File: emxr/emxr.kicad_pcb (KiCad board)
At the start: 2 copper layers, 167.9 x 76.5 mm, 137 parts, among them IC201 NJM4558D, IC301 NJM4556D, IC401 NJM2068DD, IC402 NJM4580, IC501 NJM2068DD, IC502 NJM4580, J101 POWER, J103 Bus Conn, J104 GEQ_L_PRE, J105 GEQ_L_POST, J106 GEQ_R_PRE, J107 GEQ_R_POST, J108 AUDIO_OUT, J205 InpVolL, J206 InpVolR, J208 SrcSel, J301 HPHONES, J302 HPVolL, J303 HPVolR, J401 FrontVolL, J501 FrontVolL

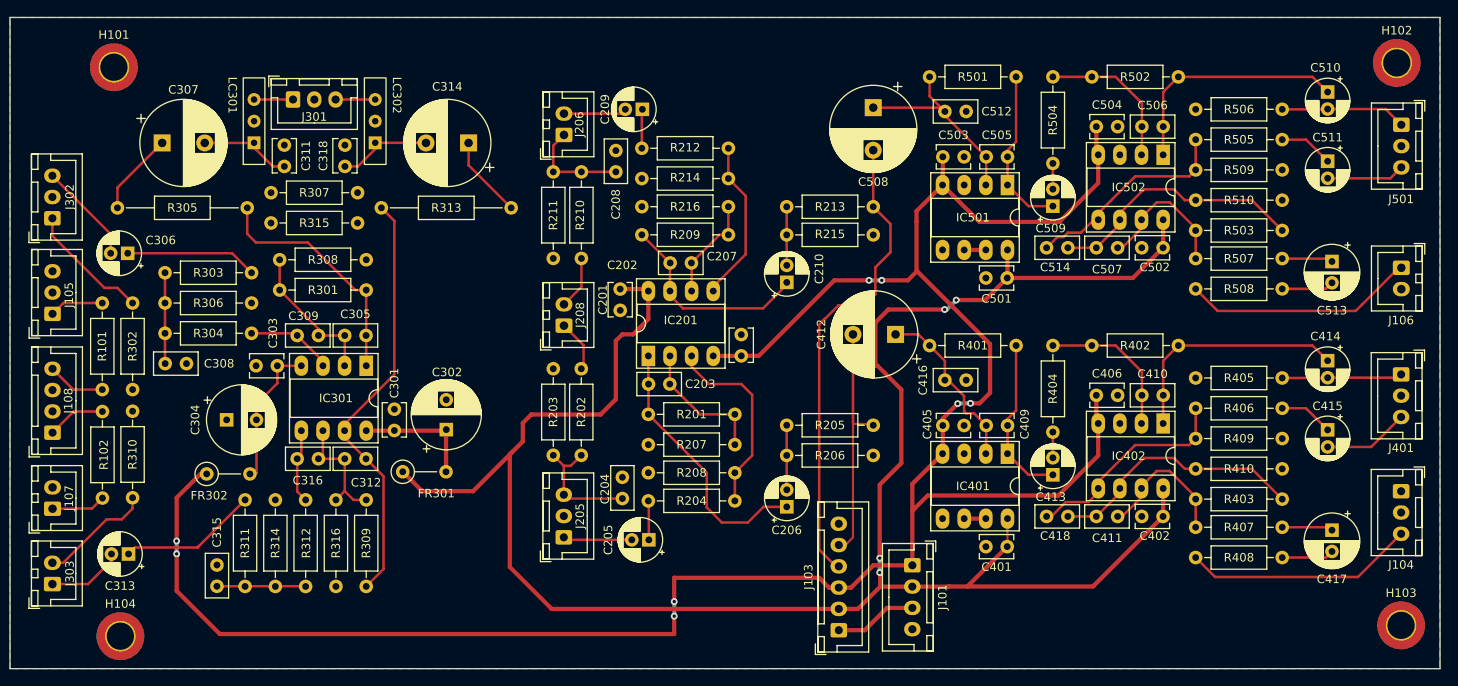
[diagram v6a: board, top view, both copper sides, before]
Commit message: change connector layout back for power
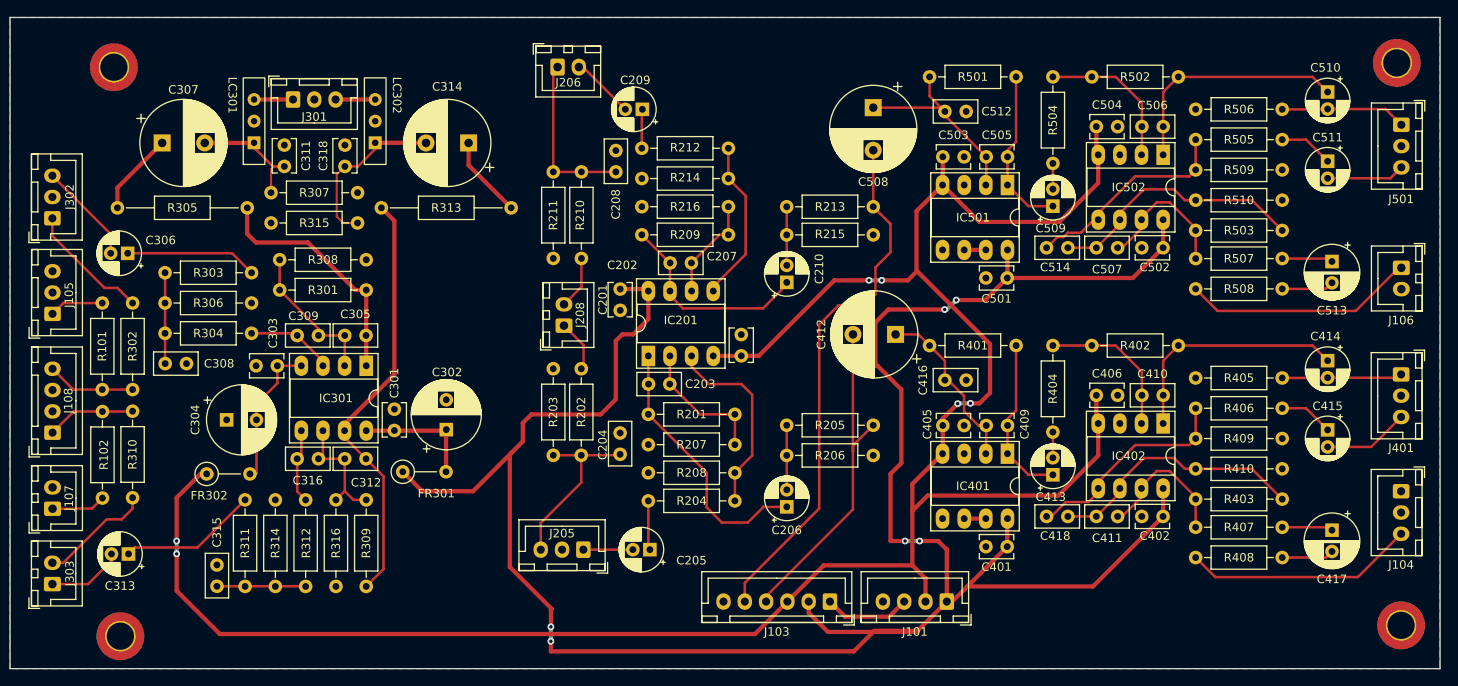
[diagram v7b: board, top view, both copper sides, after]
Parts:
- moved J206 8.00 mm to (127.0, 94.7), turned to 0 degrees
- moved J101 5.87 mm to (172.7, 157.5), turned to 180 degrees
- moved C204 5.20 mm to (134.4, 140.2)
- moved J103 3.52 mm to (159.0, 157.5), turned to 180 degrees
- moved J205 2.71 mm to (130.0, 151.4), turned to 180 degrees
- moved C205 1.16 mm to (137.9, 151.4)
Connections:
- J101 pad 1: -15V -> +15V
- J101 pad 2: +15V -> -15V
- J103 pad 4: BUS_R -> BUS_L
- J103 pad 5: BUS_L -> BUS_R
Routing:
- net +15V: track 238.1 -> 267.7 mm, vias 4 -> 6
- net BUS_L: track 28.3 -> 39.7 mm
- net Net-(C314-Pad2): track 11.1 -> 20.2 mm
- net Net-(C208-Pad1): track 12.2 -> 19.9 mm
- net Net-(C204-Pad1): track 14.8 -> 20.9 mm
- net BUS_R: track 56.8 -> 62.7 mm
- net SINGAL_L_POST_GEQ: track 6.85 -> 10.4 mm
- net SINGAL_R_POST_GEQ: track 6.89 -> 10.4 mm
- net Net-(C307-Pad2): track 11.9 -> 15.1 mm
- net Net-(C205-Pad2): track 8.11 -> 5.81 mm
- net Net-(C205-Pad1): track 4.60 -> 5.80 mm
- net SELECTED_R: track 6.96 -> 6.24 mm
- net Net-(C409-Pad1): track 21.4 -> 20.8 mm
- net -15V: track 259.4 -> 259.5 mm, vias 8 -> 6

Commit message: finished pcb draft
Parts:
- moved J205 9.76 mm to (137.7, 157.5)
- moved H104 8.16 mm to (67.6, 162.3)
- moved H101 7.13 mm to (67.8, 95.2)
- moved C205 1.98 mm to (137.7, 149.4), turned to -90 degrees
- moved H103 1.93 mm to (226.8, 162.1)
- moved H102 1.55 mm to (227.1, 94.5)
- moved C513 0.52 mm to (217.4, 117.6)
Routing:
- net Net-(C204-Pad1): track 20.9 -> 26.3 mm
- net BUS_L: track 39.7 -> 44.4 mm
- net Net-(C205-Pad1): track 5.80 -> 3.76 mm
- net Net-(C513-Pad2): track 6.14 -> 5.62 mm
- net Net-(C513-Pad1): track 5.98 -> 5.47 mm
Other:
- board size 167.9 x 76.5 mm -> 170.2 x 76.5 mm
- board text added: "FRONT VOL L"
- board text added: "FRONT VOL R"
- board text added: "GEQ L POST"
- board text added: "GEQ L PRE"
- board text added: "GEQ R PRE"
- board text added: "HP VOL L"
- board text added: "HP VOL R"
- board text added: "IN VOL L"
- board text added: "IN VOL R"
- board text added: "MIXER BUS"
- board text added: "PWR IN"
- board text added: "TO AMP"
